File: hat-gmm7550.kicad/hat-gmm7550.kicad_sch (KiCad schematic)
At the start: 12 parts, among them J1 VisionFive_GPIO, J2 Conn_01x02, J3 Conn_02x02_Odd_Even, J4 DNI, U1 CAT24C32Y

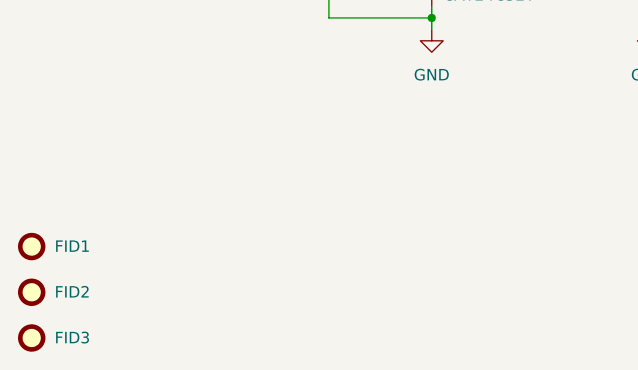
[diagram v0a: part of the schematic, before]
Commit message: Change U2 footprint due to the part availability, revision and date are updated (HAT GMM-7550)
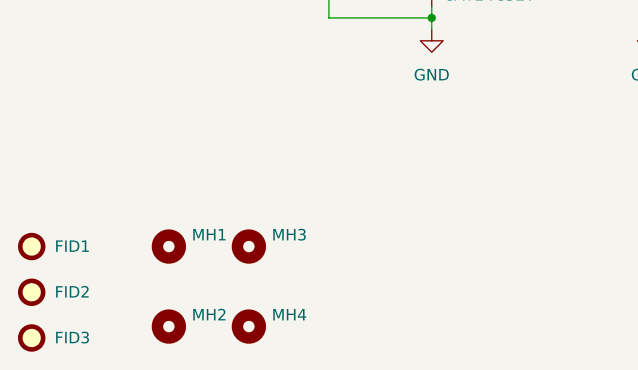
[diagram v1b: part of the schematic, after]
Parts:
- added MH1: (no value), symbol Mechanical:MountingHole
- added MH2, MH3, MH4: MountingHole, RPi_Hat:RPi_Hat_Mounting_Hole, symbol Mechanical:MountingHole
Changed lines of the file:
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@@
   (title_block
     (title "40-pin GPIO HAT adapter for GMM-7550")
-    (date "2022-03-09")
-    (rev "1.0")
+    (date "2022-04-24")
+    (rev "1.1")
   )
   (junction (at 91.44 149.86) (diameter 0) (color 0 0 0 0)
@@
     (property "Intersheet References" "${INTERSHEET_REFS}" (id 0) (at 115.8985 62.1506 0)
       (effects (font (size 1.27 1.27)) (justify left) hide)
+    )
+  )
+  (symbol (lib_id "Mechanical:MountingHole") (at 38.1 190.5 0) (unit 1)
+    (in_bom yes) (on_board yes) (fields_autoplaced)
+    (property "Reference" "MH2" (id 0) (at 40.64 189.2299 0)
+      (effects (font (size 1.27 1.27)) (justify left))
+    )
+    (property "Value" "MountingHole" (id 1) (at 40.64 191.7699 0)
+      (effects (font (size 1.27 1.27)) (justify left) hide)
+    )
+    (property "Footprint" "RPi_Hat:RPi_Hat_Mounting_Hole" (id 2) (at 38.1 190.5 0)
+      (effects (font (size 1.27 1.27)) hide)
+    )
+    (property "Datasheet" "~" (id 3) (at 38.1 190.5 0)
+      (effects (font (size 1.27 1.27)) hide)
     )
   )
@@
     (pin "1")
   )
+  (symbol (lib_id "Mechanical:MountingHole") (at 38.1 181.61 0) (unit 1)
+    (in_bom yes) (on_board yes) (fields_autoplaced)
+    (property "Reference" "MH1" (id 0) (at 40.64 180.3399 0)
+      (effects (font (size 1.27 1.27)) (justify left))
+    )
+    (property "Value" "" (id 1) (at 40.64 182.8799 0)
+      (effects (font (size 1.27 1.27)) (justify left) hide)
+    )
+    (property "Footprint" "" (id 2) (at 38.1 181.61 0)
+      (effects (font (size 1.27 1.27)) hide)
+    )
+    (property "Datasheet" "~" (id 3) (at 38.1 181.61 0)
+      (effects (font (size 1.27 1.27)) hide)
+    )
+  )
   (symbol (lib_id "Connector_Generic:Conn_02x02_Odd_Even") (at 113.03 52.07 0) (unit 1)
     (in_bom yes) (on_board yes) (fields_autoplaced)
@@
     )
   )
+  (symbol (lib_id "Mechanical:MountingHole") (at 46.99 181.61 0) (unit 1)
+    (in_bom yes) (on_board yes) (fields_autoplaced)
+    (property "Reference" "MH3" (id 0) (at 49.53 180.3399 0)
+      (effects (font (size 1.27 1.27)) (justify left))
+    )
+    (property "Value" "MountingHole" (id 1) (at 49.53 182.8799 0)
+      (effects (font (size 1.27 1.27)) (justify left) hide)
+    )
+    (property "Footprint" "RPi_Hat:RPi_Hat_Mounting_Hole" (id 2) (at 46.99 181.61 0)
+      (effects (font (size 1.27 1.27)) hide)
+    )
+    (property "Datasheet" "~" (id 3) (at 46.99 181.61 0)
+      (effects (font (size 1.27 1.27)) hide)
+    )
+  )
   (symbol (lib_id "power:+3.3V") (at 50.8 48.26 0) (unit 1)
     (in_bom yes) (on_board yes) (fields_autoplaced)
@@
     )
     (pin "1")
+  )
+  (symbol (lib_id "Mechanical:MountingHole") (at 46.99 190.5 0) (unit 1)
+    (in_bom yes) (on_board yes) (fields_autoplaced)
+    (property "Reference" "MH4" (id 0) (at 49.53 189.2299 0)
+      (effects (font (size 1.27 1.27)) (justify left))
+    )
+    (property "Value" "MountingHole" (id 1) (at 49.53 191.7699 0)
+      (effects (font (size 1.27 1.27)) (justify left) hide)
+    )
+    (property "Footprint" "RPi_Hat:RPi_Hat_Mounting_Hole" (id 2) (at 46.99 190.5 0)
+      (effects (font (size 1.27 1.27)) hide)
+    )
+    (property "Datasheet" "~" (id 3) (at 46.99 190.5 0)
+      (effects (font (size 1.27 1.27)) hide)
+    )
   )
   (symbol (lib_id "power:GND") (at 67.31 157.48 0) (unit 1)
@@
       (reference "J10") (unit 1) (value "Pmod 2x6") (footprint "Pmod:PmodSocket_2x06_P2.54mm_Horizontal")
     )
+    (path "/761c79a0-cb1a-42d4-9066-3a8bac939cdf"
+      (reference "MH1") (unit 1) (value "MountingHole") (footprint "RPi_Hat:RPi_Hat_Mounting_Hole")
+    )
+    (path "/096895d8-6d1a-4166-84e1-596cba0a2b3c"
+      (reference "MH2") (unit 1) (value "MountingHole") (footprint "RPi_Hat:RPi_Hat_Mounting_Hole")
+    )
+    (path "/7c29d288-8fce-4c84-b632-d0273027f7a5"
+      (reference "MH3") (unit 1) (value "MountingHole") (footprint "RPi_Hat:RPi_Hat_Mounting_Hole")
+    )
+    (path "/86fc755e-723f-4202-bd7f-8f17acf8da93"
+      (reference "MH4") (unit 1) (value "MountingHole") (footprint "RPi_Hat:RPi_Hat_Mounting_Hole")
+    )
     (path "/bdd97ed5-cb49-4140-9e4c-c7f96b0db717/20d9ff21-7f4c-4ffc-81a8-158b8f603059"
       (reference "MH5") (unit 1) (value "3.2mm") (footprint "MountingHole:MountingHole_3.2mm_M3_ISO7380")
@@
     )
     (path "/bdd97ed5-cb49-4140-9e4c-c7f96b0db717/d36394f9-e509-4bf8-acfb-e6199c89d6c2"
-      (reference "U2") (unit 1) (value "74LVC1G07") (footprint "Package_TO_SOT_SMD:SOT-353_SC-70-5")
+      (reference "U2") (unit 1) (value "74LVC1G07") (footprint "Package_TO_SOT_SMD:SOT-23-5")
     )
     (path "/bdd97ed5-cb49-4140-9e4c-c7f96b0db717/22418fb5-4b10-4bd8-bdf8-5b94117a6fb1"

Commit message: Update designs to KiCad v7
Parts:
- MH1: value (none) -> MountingHole; footprint (none) -> RPi_Hat:RPi_Hat_Mounting_Hole

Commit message: Update copyright years and increment revision
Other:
- note added: "Copyright (c) 2022-2024 Anton Kuzmin Licensed under CERN-OHL-P v2 https://github.com/gmm-7550/"
- note removed: "Copyright (c) 2022 Anton Kuzmin Licensed under CERN-OHL-P v2 https://github.com/ak-fau/gmm7550.git"
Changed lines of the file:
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@@
   (title_block
     (title "40-pin GPIO HAT adapter for GMM-7550")
-    (date "2022-04-24")
-    (rev "1.1")
+    (date "2024-01-27")
+    (rev "1.2")
   )
   (junction (at 91.44 149.86) (diameter 0) (color 0 0 0 0)
@@
     (stroke (width 0) (type default))
   )
-  (text "Copyright (c) 2022  Anton Kuzmin\nLicensed under CERN-OHL-P v2\nhttps://github.com/ak-fau/gmm7550.git"
+  (text "Copyright (c) 2022-2024  Anton Kuzmin\nLicensed under CERN-OHL-P v2\nhttps://github.com/gmm-7550/"
     (at 198.12 179.07 0)
     (effects (font (size 2.54 2.54)) (justify left bottom))
